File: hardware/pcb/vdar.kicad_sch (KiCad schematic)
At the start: 8 parts, among them M1 Stepper_Motor_bipolar, M2 Stepper_Motor_bipolar, SW1 SW_Nidec_CAS-120A1, SW2 SW_Nidec_CAS-120A1, U1 ESP32-DEVKITC, U3 TMC2209-LA, U4 TMC2209-LA, U5 TSR_1-2450

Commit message: Update Everything
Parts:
- removed SW1, SW2: SW_Nidec_CAS-120A1, Button_Switch_SMD:Nidec_Copal_CAS-120A, symbol Switch:SW_Nidec_CAS-120A1
- removed U3, U4: TMC2209-LA, Package_DFN_QFN:VQFN-28-1EP_5x5mm_P0.5mm_EP3.7x3.7mm_ThermalVias, symbol Driver_Motor:TMC2209-LA
- removed U5: TSR_1-2450, Converter_DCDC:Converter_DCDC_TRACO_TSR-1_THT, symbol Converter_DCDC:TSR_1-2450
- added C1: 16V 10uF, easyeda2kicad:C1206, symbol easyeda2kicad:CL31A106KOHNNNE
- added C2, C3, C4, C6: 100V 100nF, easyeda2kicad:C1206, symbol easyeda2kicad:CL31B104KCFNNNE
- added C5, C7: 35V 470muF, easyeda2kicad:CAP-SMD_BD10.0-L10.3-W10.3-LS11.0-FD, symbol easyeda2kicad:RVT470UF35V67RV0056
- added D1: 15Vrwm 16.7Vbr 24.4VC, easyeda2kicad:SMB_L4.6-W3.6-LS5.3-RD, symbol easyeda2kicad:SMBJ15A_C83846
- added H1, H2, H3, H4: MountingHole, easyeda2kicad:MountingHole_3.2mm_M3_Clearance, symbol Mechanical:MountingHole
- added J1: USB C PD Board 12V 5A, easyeda2kicad:USB_C_PD_BOARD, symbol Connector:USB_C_Receptacle_PowerOnly_6P
- added J2, J3: Optical Endstop, Connector_JST:JST_PH_B3B-PH-K_1x03_P2.00mm_Vertical, symbol Connector_Generic:Conn_01x03
- added J4: TF-LUNA, Connector_JST:JST_PH_B8B-PH-K_1x08_P2.00mm_Vertical, symbol Connector_Generic:Conn_01x08
- added JP1: SolderJumper_2_Open, Jumper:SolderJumper-2_P1.3mm_Open_TrianglePad1.0x1.5mm, symbol Jumper:SolderJumper_2_Open
- added JP2, JP3: SolderJumper_3_Open, Jumper:SolderJumper-3_P2.0mm_Open_TrianglePad1.0x1.5mm_NumberLabels, symbol Jumper:SolderJumper_3_Open
- added R1: 1000Ω, easyeda2kicad:R1206, symbol easyeda2kicad:FRC1206J102TS
- added U2: MP1584EN Buck Converter, easyeda2kicad:MP1584EN, symbol Converter_DCDC:Ag9905LP
- added U3, U4: TMC2209_SILENTSTEPSTICK, TMC2209_SILENTSTEPSTICK:MODULE_TMC2209_SILENTSTEPSTICK_INTERNAL SILKSCREEN, symbol TMC2209_SILENTSTEPSTICK:TMC2209_SILENTSTEPSTICK
- M1, M2: value Stepper_Motor_bipolar -> Nema 17; footprint (none) -> Connector_JST:JST_PH_B4B-PH-K_1x04_P2.00mm_Vertical
- U1: footprint ESP32-DEVKITC:MODULE_ESP32-DEVKITC -> ESP32-DEVKITC:MODULE_ESP32-DEVKITC_VDAR
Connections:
- net 5V is gone; now on net 3.3V: U1.19 (EXT_5V)
- net 3.3V: now also C1.1, C2.1, C3.1, C4.1, C6.1, J2.1 (Pin_1), J3.1 (Pin_1), J4.1 (Pin_1), U2.1 (+VDC), U3.2 (VIO), U4.15 (MS1), U4.2 (VIO)
- net GND: now also U1.32 (GND2), U1.38 (GND3), C1.2, C2.2, C3.2, C4.2, C5.2, C6.2, C7.2, D1.2, J1.A12 (GND), J2.3 (Pin_3), J3.3 (Pin_3), J4.4 (Pin_4), U2.3 (-VDC), U2.7 (VIN-), U3.1 (GND), U3.14 (MS2), U3.15 (MS1), U3.7 (GND), U4.1 (GND), U4.14 (MS2), U4.7 (GND)
- net M1A_1: now reaches M1.1 (-)
- net M1A_1: now also U3.5 (M1A)
- net M1B_1: now reaches M1.2
- net M1B_1: now also U3.4 (M1B)
- net M2A_1: now reaches M1.3
- net M2A_1: now also U3.6 (M2A)
- net M2B_1: now reaches M1.4
- net M2B_1: now also U3.3 (M2B)
- net M1A_2: now reaches M2.1 (-)
- net M1A_2: now also U4.5 (M1A)
- net M1B_2: now reaches M2.2
- net M1B_2: now also U4.4 (M1B)
- net M2A_2: now reaches M2.3
- net M2A_2: now also U4.6 (M2A)
- net M2B_2: now reaches M2.4
- net M2B_2: now also U4.3 (M2B)
- net EN: now reaches U1.10 (IO26)
- net EN: now also U3.16 (~{EN}), U4.16 (~{EN})
- net at U1.27 (IO16): now also JP1.1 (A)
- net ESP-TMC: now reaches U1.28 (IO17)
- net ESP-TMC: now also JP2.2 (C), JP3.2 (C), R1.2
- net LUNA-ESP: now reaches U1.30 (IO18)
- net LUNA-ESP: now also J4.3 (Pin_3)
- net ESP-LUNA: now reaches U1.31 (IO19)
- net ESP-LUNA: now also J4.2 (Pin_2)
- net LIM2: now reaches U1.36 (IO22)
- net LIM2: now also J3.2 (Pin_2)
- net LIM1: now reaches U1.37 (IO23)
- net LIM1: now also J2.2 (Pin_2)
- net SIG1: no longer names the net of U1.12 (IO14)
- net SIG2: no longer names the net of U1.11 (IO27)
- new net: JP1.2 (B), R1.1
- new net: JP2.1 (A), U3.12 (UART)
- new net: JP2.3 (B), U3.13 (PDN)
- new net: JP3.1 (A), U4.12 (UART)
- new net: JP3.3 (B), U4.13 (PDN)
- new net 12V: C5.1, C7.1, D1.1, J1.A9 (VBUS), U2.5 (VIN+), U3.8 (VM), U4.8 (VM)
- no-connect marks 0 -> 37
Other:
- moved on the sheet: M1, U1

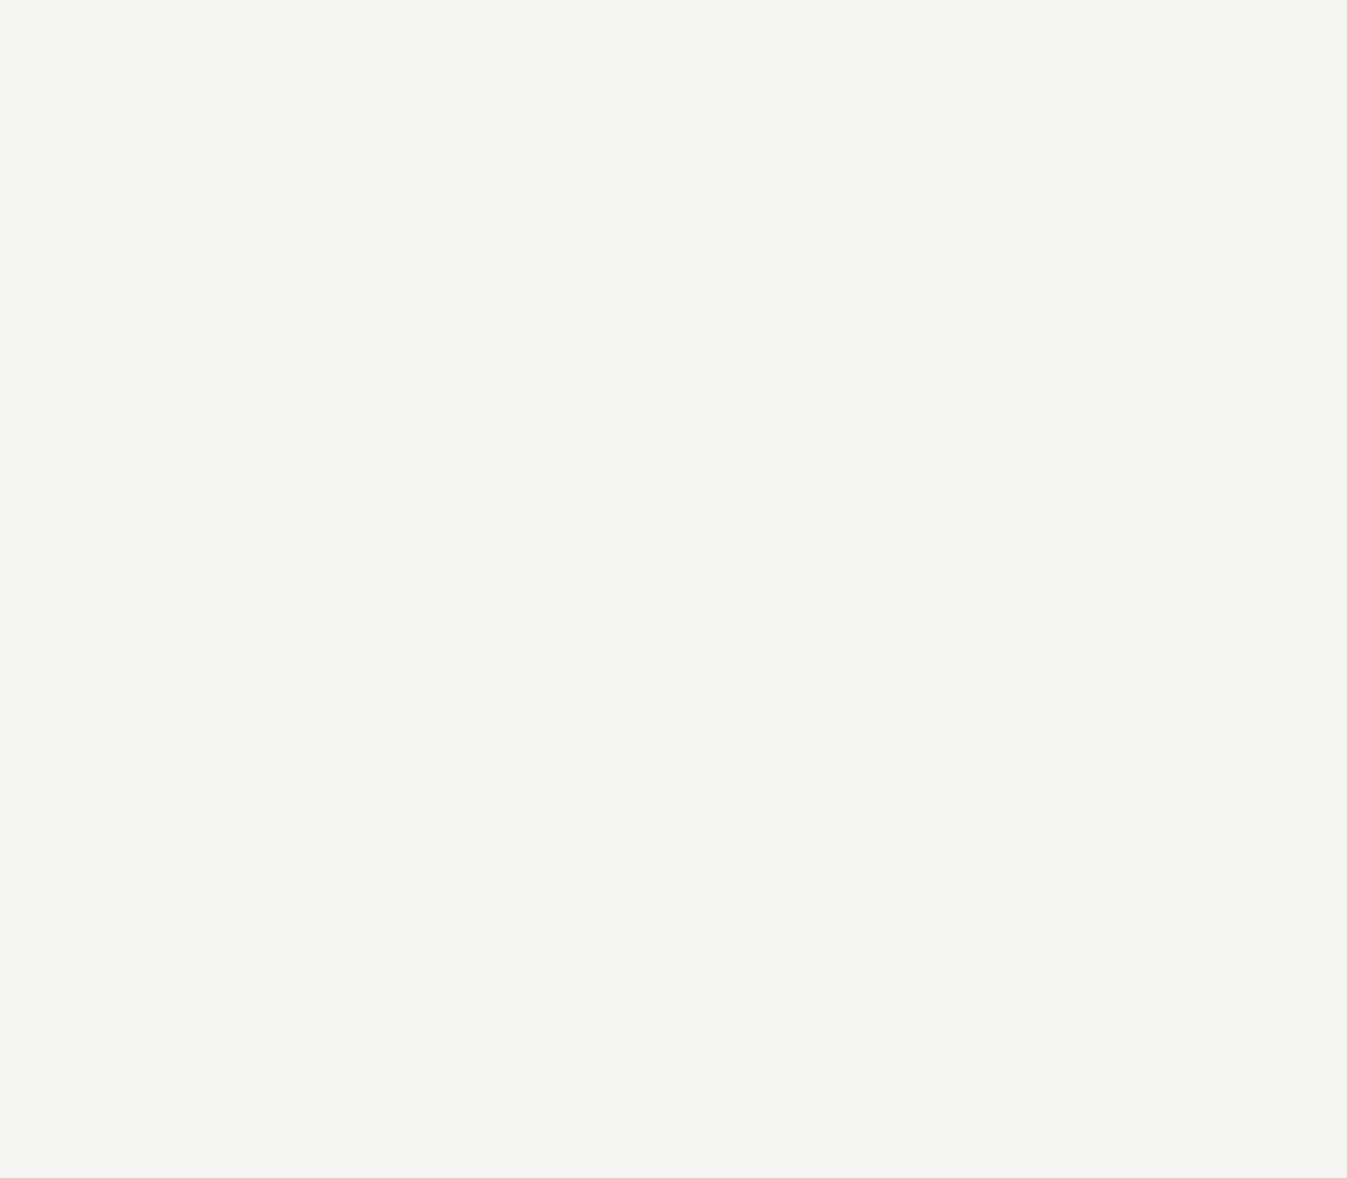
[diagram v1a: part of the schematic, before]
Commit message: Add offboard wiring schematic
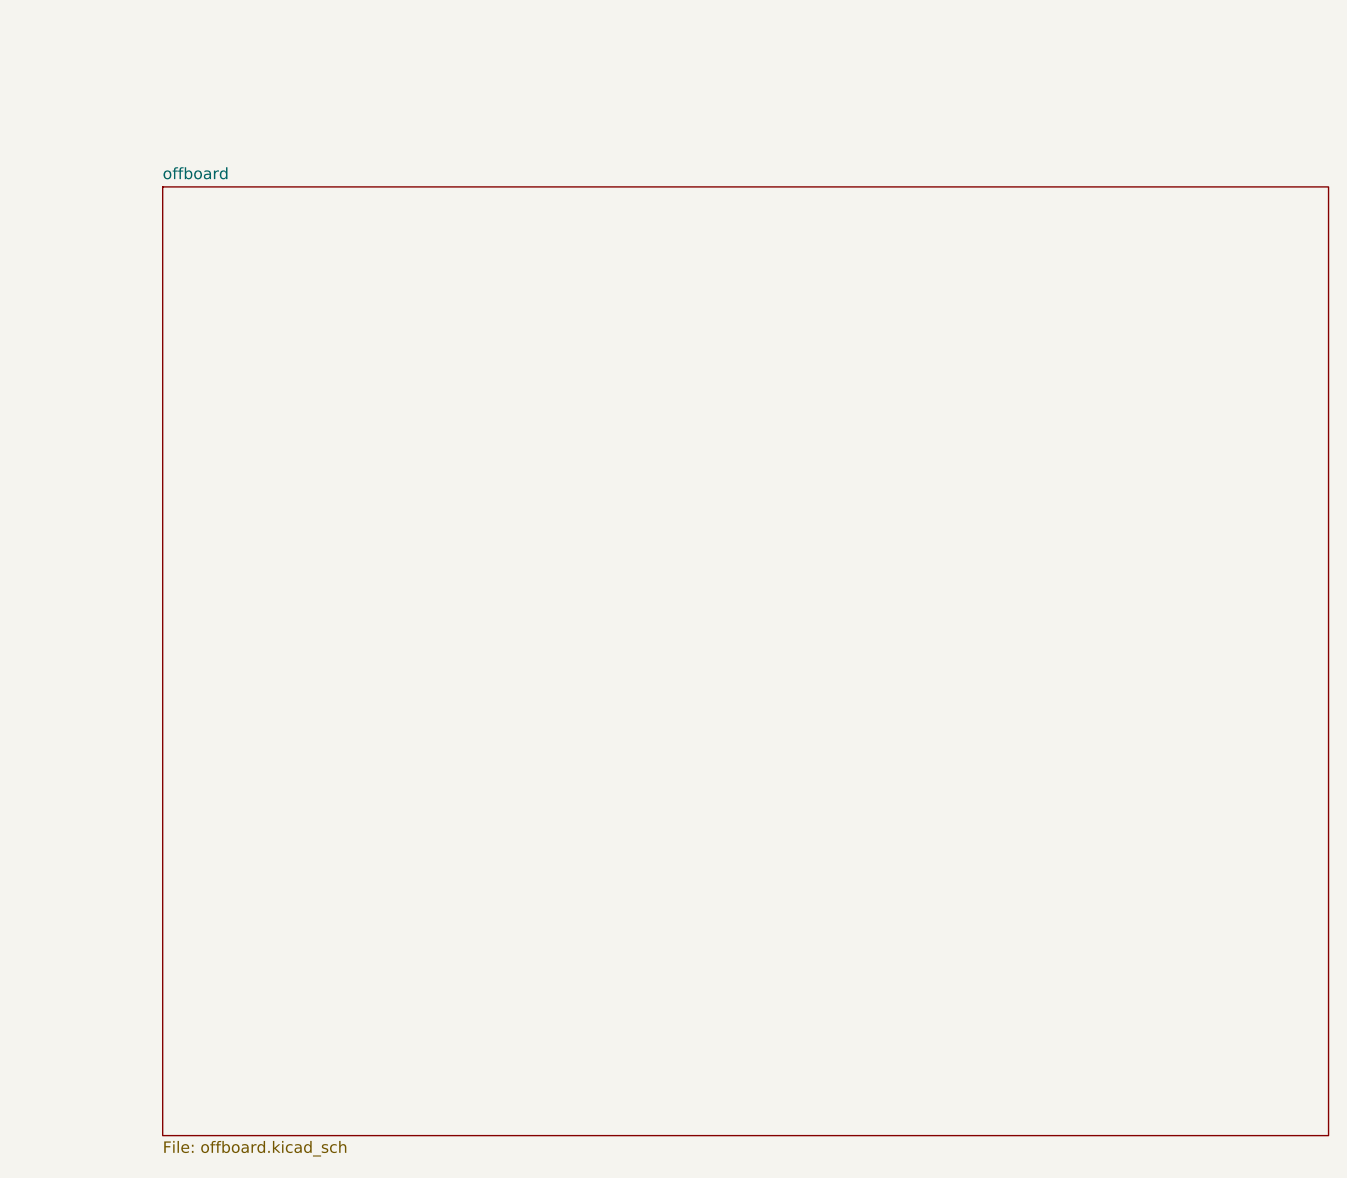
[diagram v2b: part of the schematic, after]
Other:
- added sheet offboard (offboard.kicad_sch)
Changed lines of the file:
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@@
+		)
+	)
+	(sheet
+		(at 297.18 52.07)
+		(size 129.54 105.41)
+		(exclude_from_sim yes)
+		(in_bom no)
+		(on_board no)
+		(dnp yes)
+		(fields_autoplaced yes)
+		(stroke
+			(width 0.1524)
+			(type solid)
+		)
+		(fill
+			(color 0 0 0 0)
+		)
+		(property "Sheetname" "offboard"
+			(at 297.18 51.3584 0)
+			(show_name no)
+			(do_not_autoplace no)
+			(effects
+				(font
+					(size 1.27 1.27)
+				)
+				(justify left bottom)
+			)
+		)
+		(property "Sheetfile" "offboard.kicad_sch"
+			(at 297.18 158.0646 0)
+			(show_name no)
+			(do_not_autoplace no)
+			(effects
+				(font
+					(size 1.27 1.27)
+				)
+				(justify left top)
+			)
+		)
+		(instances
+			(project "vdar"
+				(path "/8db2f348-90b2-424a-8046-601e82624cf2"
+					(page "2")
+				)
+			)
 		)
 	)
